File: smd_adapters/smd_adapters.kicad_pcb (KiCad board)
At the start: 2 copper layers, 79.8 x 69.7 mm, 34 parts

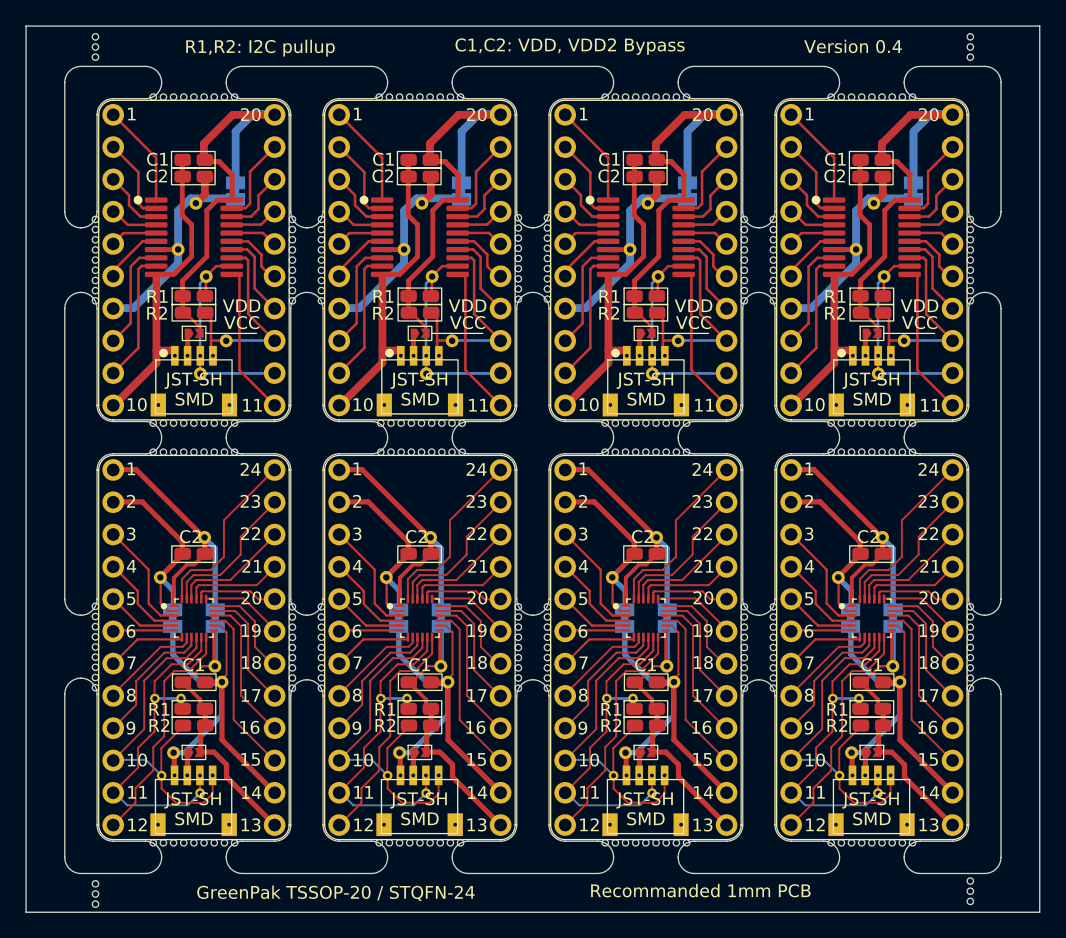
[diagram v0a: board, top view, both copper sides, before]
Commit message: Simplified the paneling: removed the horizontal tabs.
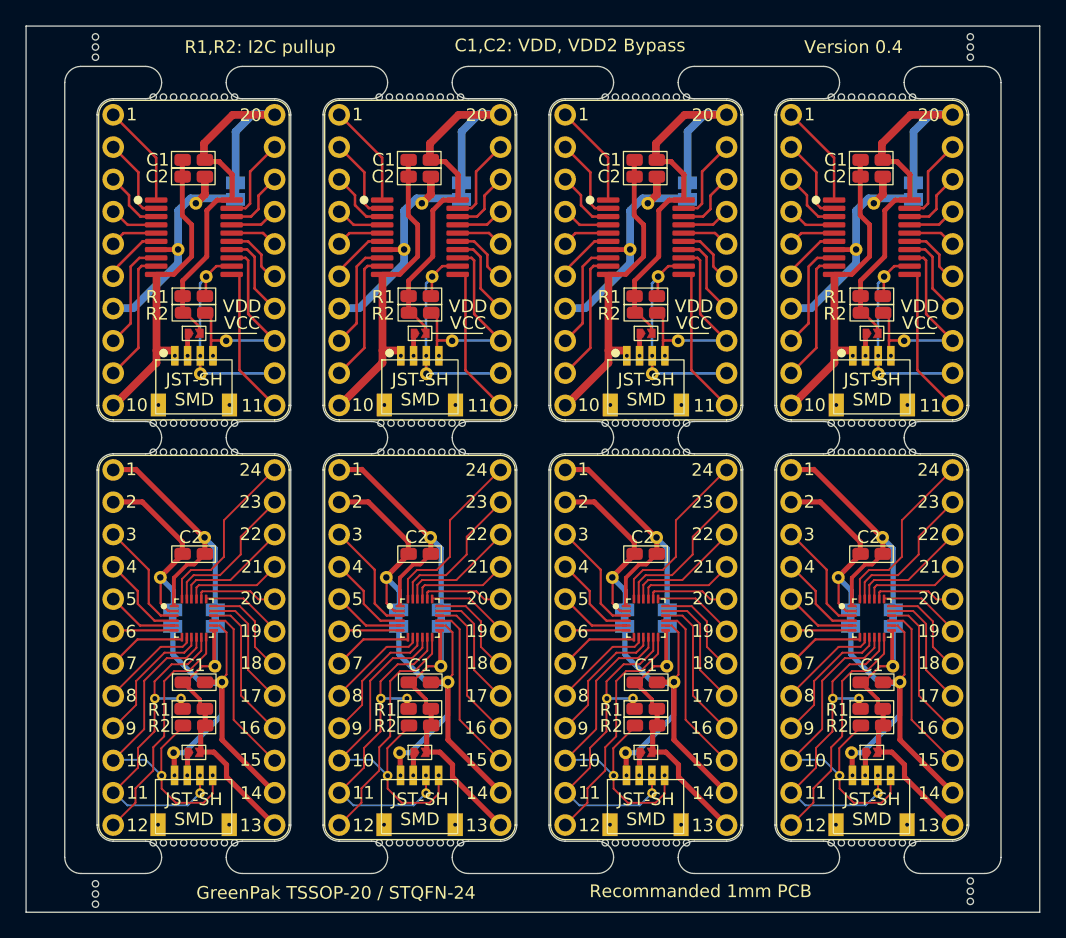
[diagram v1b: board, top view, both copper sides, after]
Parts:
- removed the mouse-bite-2.54mm-slot at (-14.5, -21.1)
- removed the mouse-bite-2.54mm-slot at (-32.3, 9.36)
- removed the mouse-bite-2.54mm-slot at (21.1, 9.40)
- removed the mouse-bite-2.54mm-slot at (-14.5, 9.40)
- removed the mouse-bite-2.54mm-slot at (38.9, 9.40)
- removed the mouse-bite-2.54mm-slot at (-32.3, -21.1)
- removed the mouse-bite-2.54mm-slot at (3.30, -21.2)
- removed the mouse-bite-2.54mm-slot at (3.30, 9.40)
- removed the mouse-bite-2.54mm-slot at (21.1, -21.1)
- removed the mouse-bite-2.54mm-slot at (38.9, -21.1)
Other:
- outline, holes or cut-outs redrawn
